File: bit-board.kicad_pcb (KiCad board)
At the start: 4 copper layers, 85 x 56 mm, 209 parts, among them M1 FDV301N, M1A NX3008PBK, M1B2 FDV301N, M1B3 FDV301N, M1BF NX3008PBK, M1BG NX3008PBK, M1DE FDV301N, M1L0 FDV301N, M1L1 FDV301N, M1L2 FDV301N, M1L3 FDV301N, M1MAG FDV301N, M1NAF FDV301N, M1NAG FDV301N, M1NEE FDV301N, M1NL FDV301N, M1NS4 FDV301N, M1OEE FDV301N, M1ON FDV301N, M1S5 FDV301N, M1S6 FDV301N, M1S7 FDV301N, M1S8 FDV301N, M1S9 FDV301N, M1XE FDV301N, M2 FDV301N, M2A FDV301N, M2B2 NX3008PBK, M2B3 NX3008PBK, M2BF FDV301N, M2BG FDV301N, M2DE FDV301N, M2L0 FDV301N, M2L1 FDV301N, M2L2 FDV301N, M2L3 FDV301N, M2MAG FDV301N, M2NAF FDV301N, M2NAG FDV301N, M2NEE FDV301N, M2NL FDV301N, M2NS4 FDV301N, M2OEE FDV301N, M2ON FDV301N, M2S5 FDV301N, M2S6 FDV301N, M2S7 FDV301N, M2S8 FDV301N, M2S9 FDV301N, M2XE FDV301N, M3 FDV301N, M3A NX3008PBK, M3BF NX3008PBK, M3BG NX3008PBK, M3OEE FDV301N, M3ON FDV301N, M3XE FDV301N, M4 FDV301N, M4A FDV301N, M4BF FDV301N, M4BG FDV301N, M4XE FDV301N, Q1BF PDTC124TU, Q1BG PDTC124TU, Q1K PDTC124TU, Q1L0 PDTC124TU, Q1L1 PDTC124TU, Q1L2 PDTC124TU, Q1L3 PDTC124TU, Q1R PDTC124TU, Q1U PDTC124TU, Q1X PDTC124TU, Q1Y PDTC124TU, Q2A PDTC124TU, Q2BF PDTC124TU, Q2BG PDTC124TU, Q2K PDTC124TU, Q2L0 PDTC124TU, Q2L1 PDTC124TU, Q2L2 PDTC124TU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

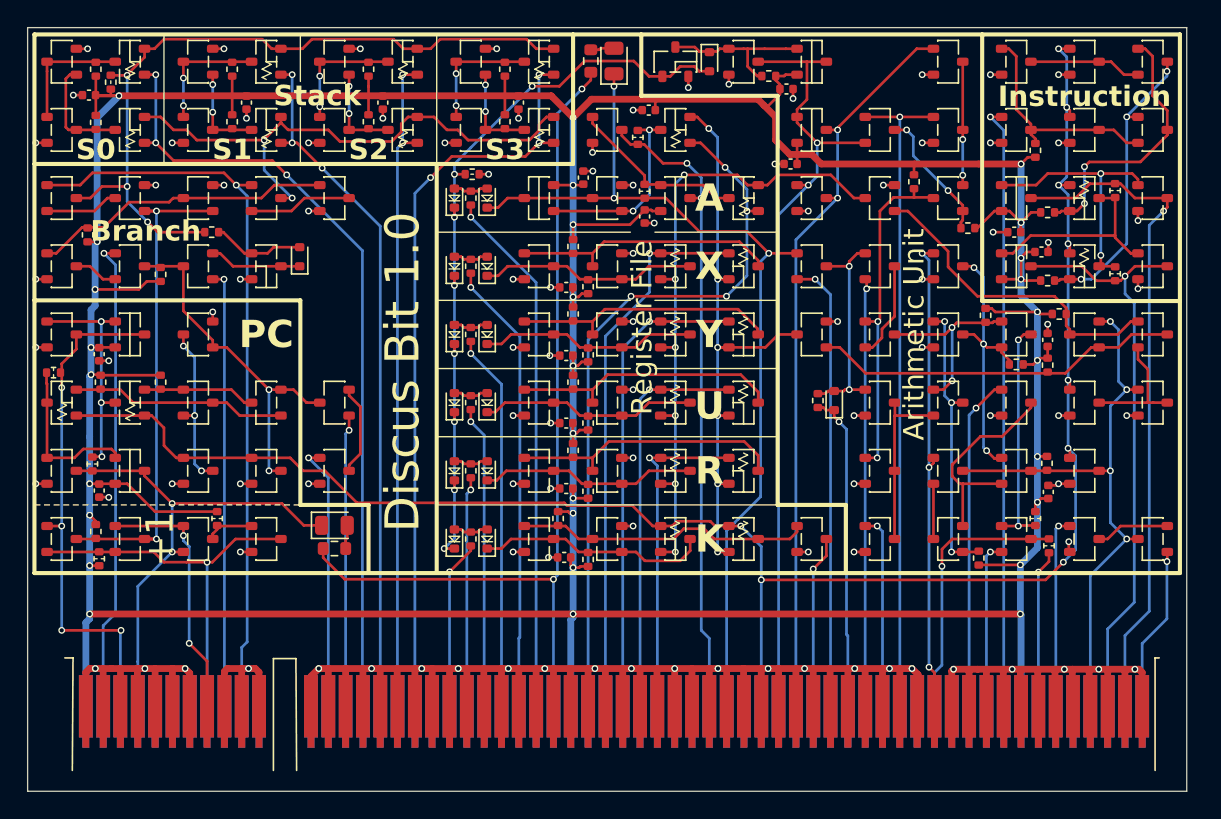
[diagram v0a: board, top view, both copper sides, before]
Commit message: Optimize for base board routing.
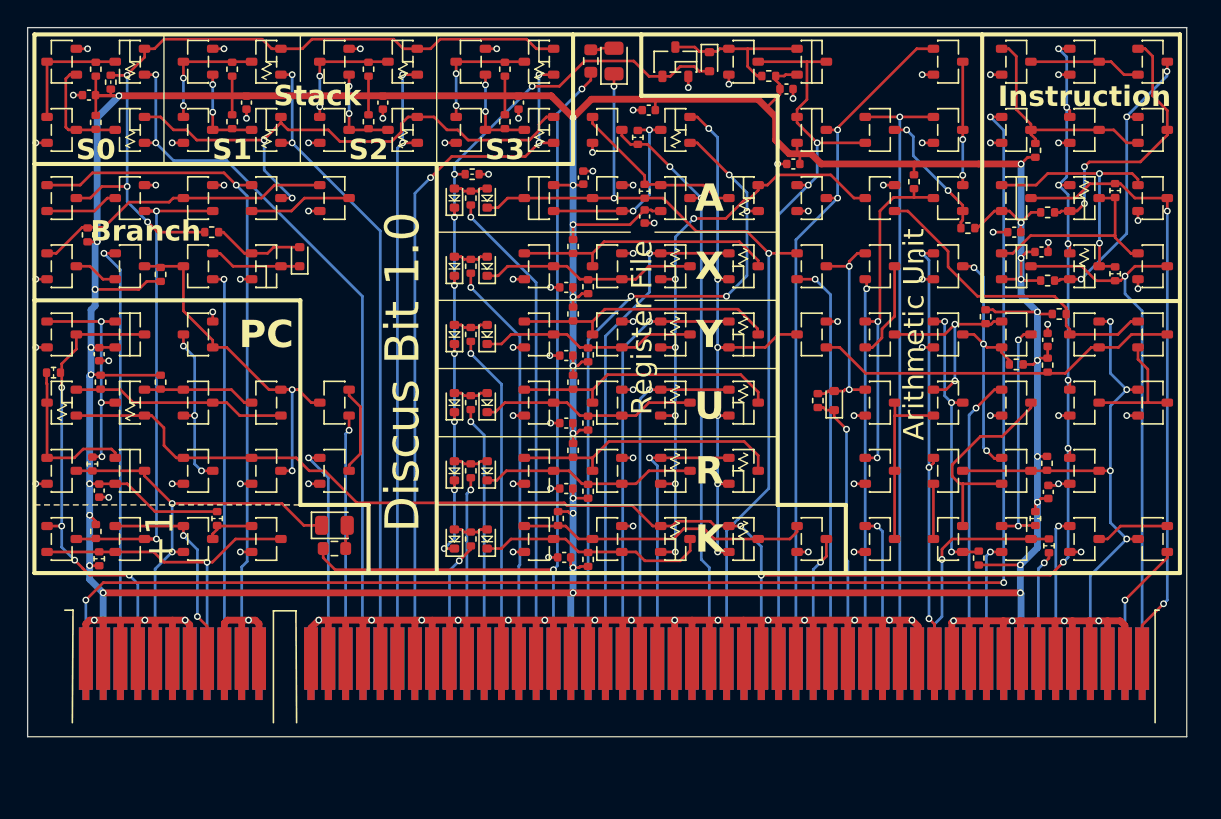
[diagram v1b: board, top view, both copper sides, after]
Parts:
- moved JMAIN 3.50 mm to (143.0, 92.6)
- moved C18 0.20 mm to (156.2, 55.0)
- moved RDE 0.10 mm to (170.2, 66.2)
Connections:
- JMAIN pad A1: Vdd -> O
- JMAIN pad A2: Inc -> Vdd
- JMAIN pad A3: P -> Inc
- JMAIN pad A4: P# -> P
- JMAIN pad A5: (no net) -> P#
- JMAIN pad A54: O -> (no net)
- JMAIN pad A60: I -> (no net)
- JMAIN pad A61: I# -> K#
- JMAIN pad A62: K# -> I
- JMAIN pad B62: GND -> I#
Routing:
- net O: track 44.5 -> 107.5 mm, vias 1 -> 3
- net Vdd: track 365.7 -> 354.2 mm
- net S0: track 58.5 -> 53.0 mm, vias 3 -> 2
- net Ao: track 47.4 -> 43.0 mm
- net GND: track 288.0 -> 283.9 mm, vias 100 -> 99
- net phi: track 133.4 -> 129.3 mm
- net I: track 43.5 -> 39.4 mm
- net P#: track 36.6 -> 32.6 mm
- net I#: track 49.4 -> 45.4 mm, vias 1 -> 2
- net P: track 38.2 -> 34.3 mm
- net Bling: track 65.8 -> 62.1 mm
- net OR: track 31.4 -> 27.7 mm
- net Inc: track 34.8 -> 31.0 mm
- net S1: track 50.9 -> 47.1 mm, vias 3 -> 2
- net WA: track 53.3 -> 49.6 mm
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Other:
- board size 85 x 56 mm -> 85 x 52 mm

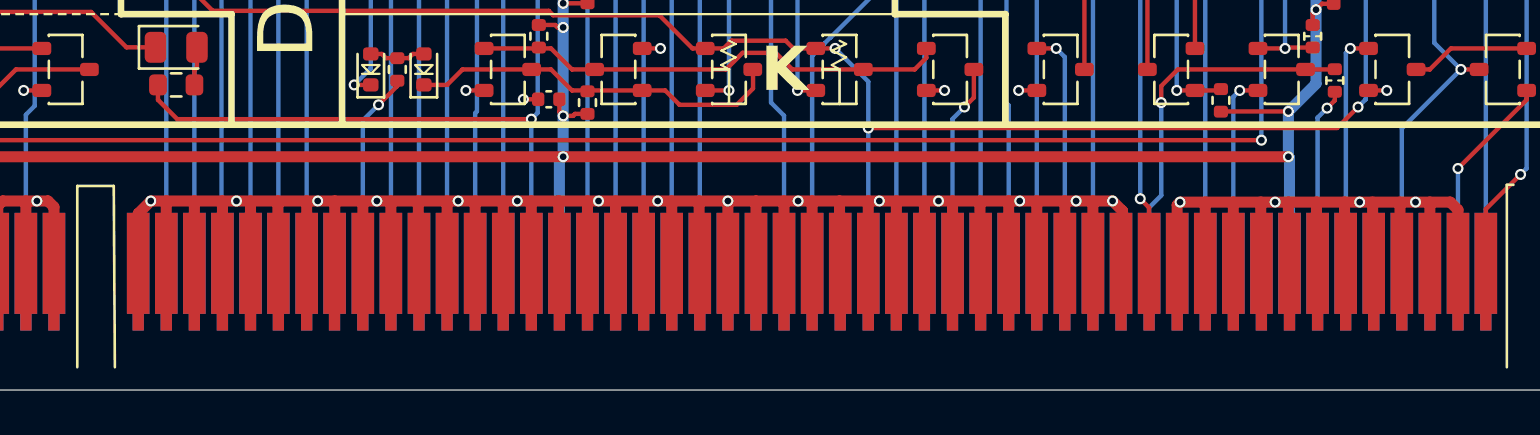
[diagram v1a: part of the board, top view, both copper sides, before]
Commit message: Rename footprints to be more systematic.
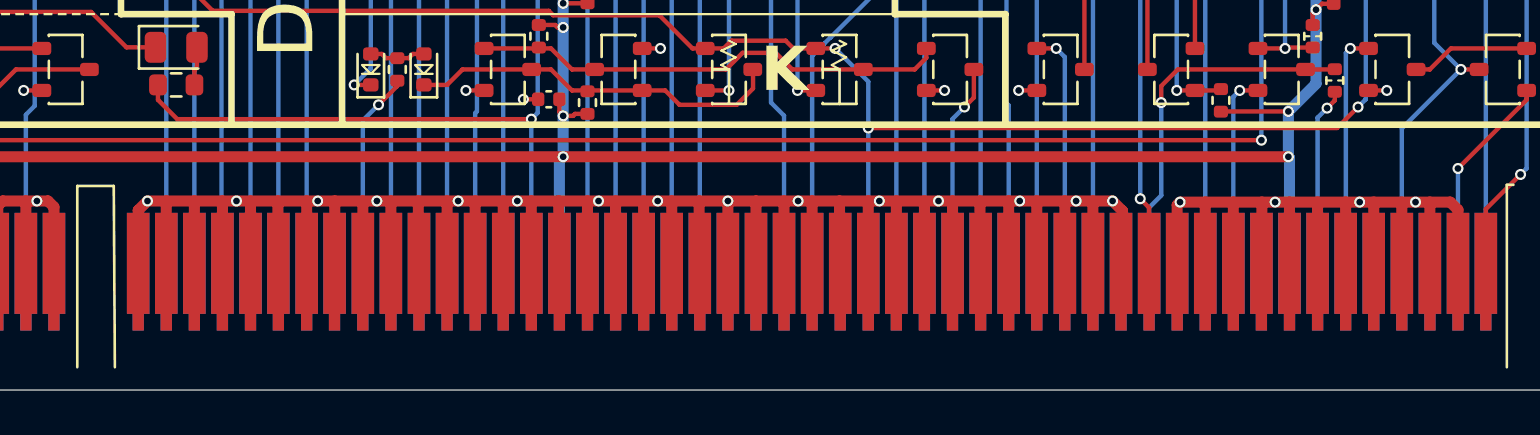
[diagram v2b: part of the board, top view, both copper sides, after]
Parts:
- C1, C10, C11, C12, C13, C14, C15, C16, C17, C18, C19, C2, C20, C3, C4, C5, C6, C7, C8, C9: footprint Parts:0402w -> Parts:C_0402
- M1, M1B2, M1B3, M1DE, M1L0, M1L1, M1L2, M1L3, M1MAG, M1NAF, M1NAG, M1NEE, M1NL, M1NS4, M1OEE, M1ON, M1S5, M1S6, M1S7, M1S8, M1S9, M1XE, M2, M2A, M2BF, M2BG, M2DE, M2L0, M2L1, M2L2, M2L3, M2MAG, M2NAF, M2NAG, M2NEE, M2NL, M2NS4, M2OEE, M2ON, M2S5, M2S6, M2S7, M2S8, M2S9, M2XE, M3, M3OEE, M3ON, M3XE, M4, M4A, M4BF, M4BG, M4XE, MAF, ME, MI3, MI5, MIAF, MIAG, MIE, MIK, MIL, MIR, MIS4, MIU, MIX, MIY, MJAF, MJAG, MJK, MJL, MJR, MJU, MJX, MJY, ML, MNN, MPE, MPS4: footprint Parts:sot23-nmos -> Parts:SOT23_nmos
- M1A, M1BF, M1BG, M2B2, M2B3, M3A, M3BF, M3BG: footprint Parts:sot23-pmos -> Parts:SOT23_pmos
- Q1BF, Q1BG, Q1K, Q1L0, Q1L1, Q1L2, Q1L3, Q1R, Q1U, Q1X, Q1Y, Q2A, Q2BF, Q2BG, Q2K, Q2L0, Q2L1, Q2L2, Q2L3, Q2R, Q2U, Q2X, Q2Y, Q3A: footprint Parts:sot323-bjt -> Parts:SOT23_bias
- Q3, QI4: footprint Parts:sot323-hbt -> Parts:SOT23_bjt
- R1, R2: footprint Parts:0603-pull -> Parts:R_0402_pull
- R1A, R1BF, R1BG, R2A, R2BF, R2BG, RIE, RIS4, RPE, RPS4: footprint Parts:0603-strong -> Parts:R_0402_strong
- R1K, R1L0, R1L1, R1L2, R1L3, R1R, R1U, R1X, R1Y, R2L0, R2L1, R2L2, R2L3, R3A, R6, RDE, RI3, RI4, RI5, RIAF, RIAG, RIK, RIL, RIR, RIU, RIX, RIY, RJAF, RJAG, RJK, RJL, RJR, RJU, RJX, RJY, RMAG, RNEE, RNN, RNS4, ROEE, RON, RS6, RXE: footprint Parts:0603-load -> Parts:R_0402_load

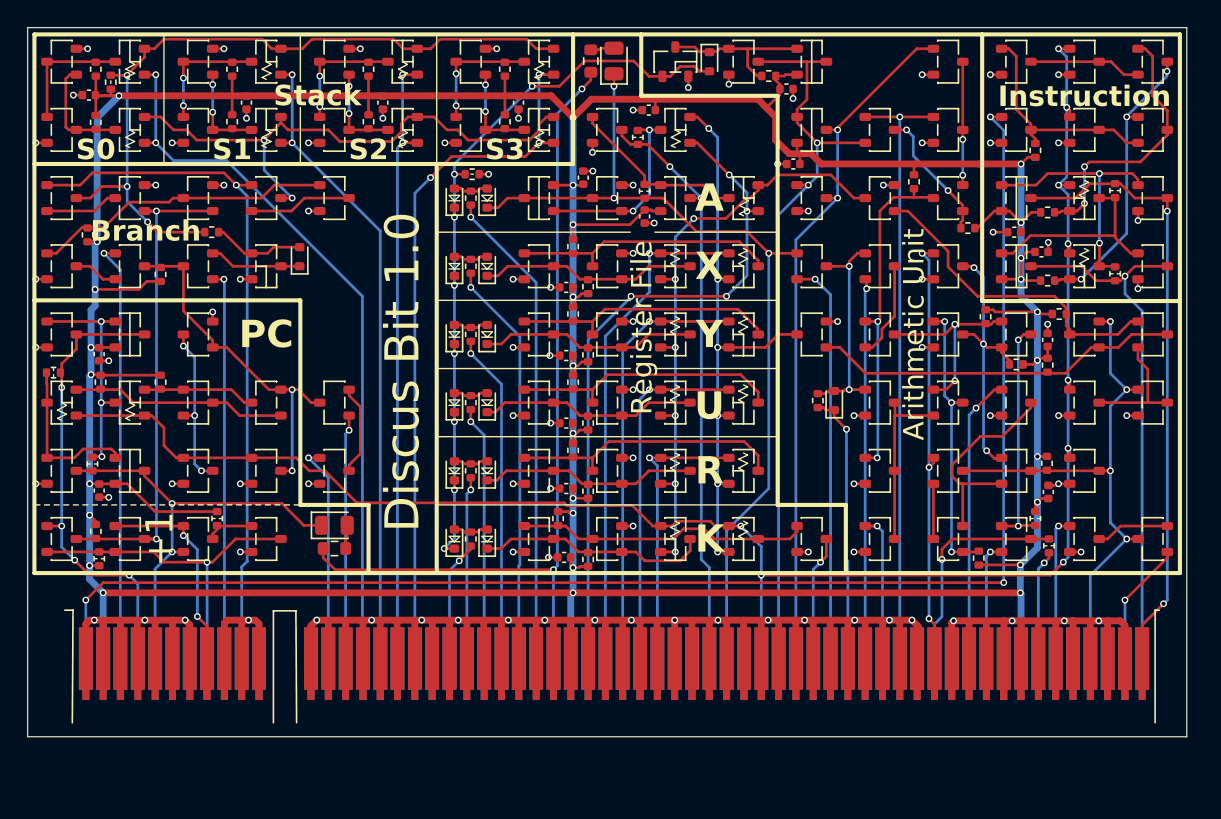
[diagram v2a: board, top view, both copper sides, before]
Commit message: Shuffle the connector.
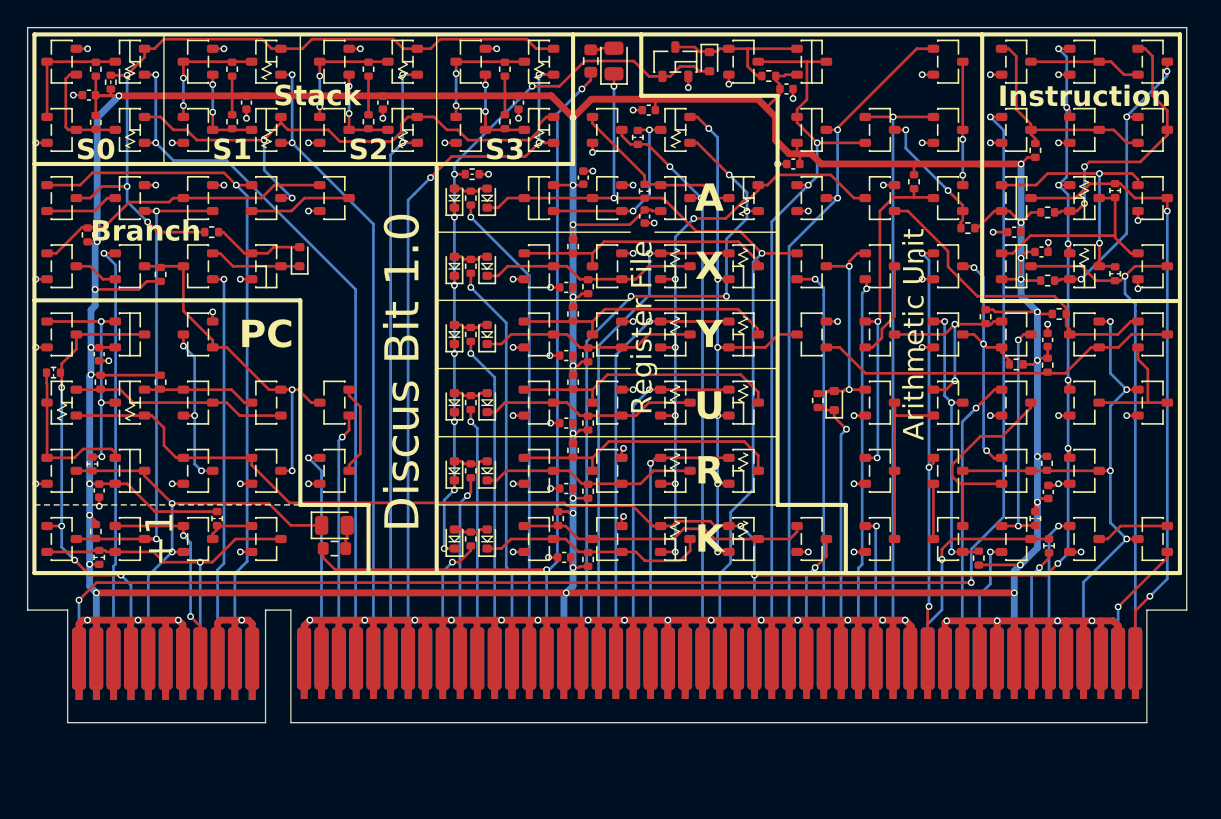
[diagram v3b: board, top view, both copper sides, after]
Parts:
- moved JMAIN 0.50 mm to (142.5, 92.6)
- moved RPS4 0.10 mm to (105.2, 83.8)
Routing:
- net O: track 107.5 -> 106.6 mm
- net P: track 34.3 -> 33.7 mm
- net WR: track 20.7 -> 20.2 mm
- net RK: track 8.91 -> 9.41 mm
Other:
- board size 85 x 52 mm -> 85 x 51 mm
